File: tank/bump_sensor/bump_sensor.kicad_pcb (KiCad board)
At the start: 2 copper layers, 77.5 x 11.2 mm, 5 parts, among them J1 Conn_01x02_Male, SW1 SW_SPDT, SW2 SW_SPDT

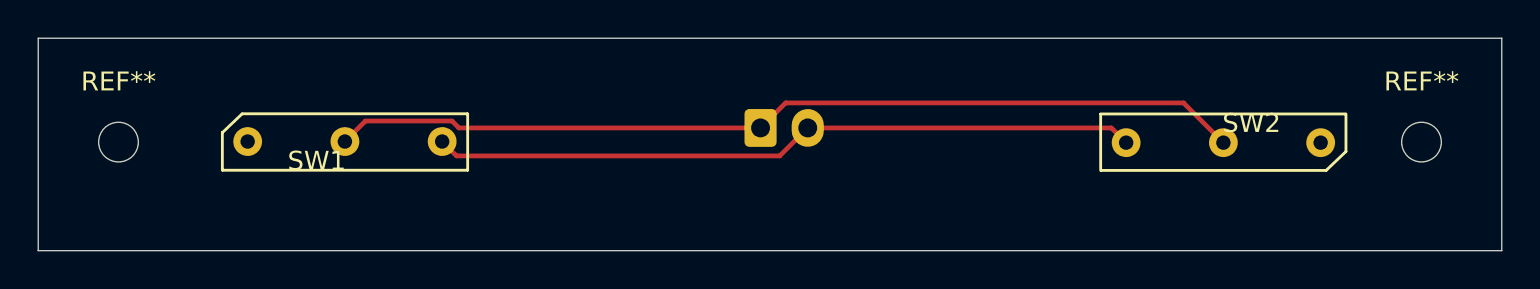
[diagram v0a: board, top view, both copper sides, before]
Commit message: Bump Sensor Version 0.2 - make contact switch thru-holes bigger
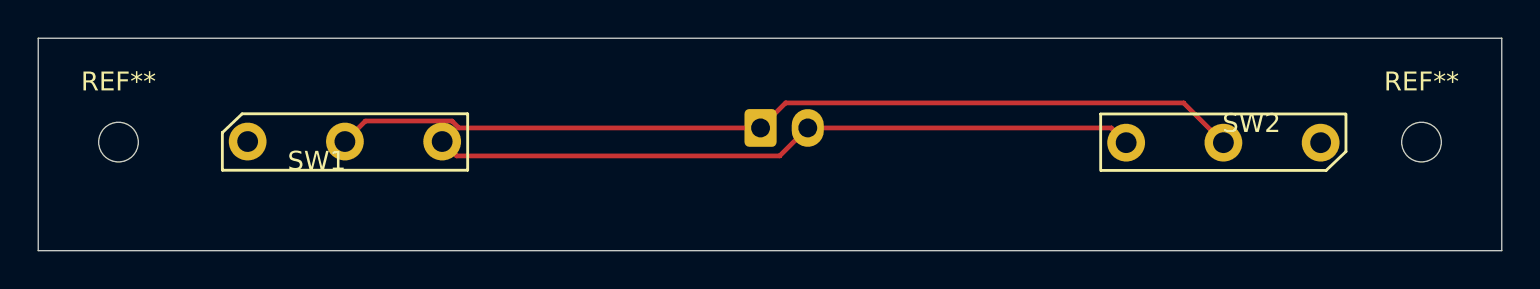
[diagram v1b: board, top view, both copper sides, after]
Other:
- board text added: "Laser Tag Robot Tank Bump Sensor 0.2 M.I.A.R. Labs nick.groesz@gmail.com"
- board text removed: "Laser Tag Robot Tank Bump Sensor 0.1 M.I.A.R. Labs nick.groesz@gmail.com"

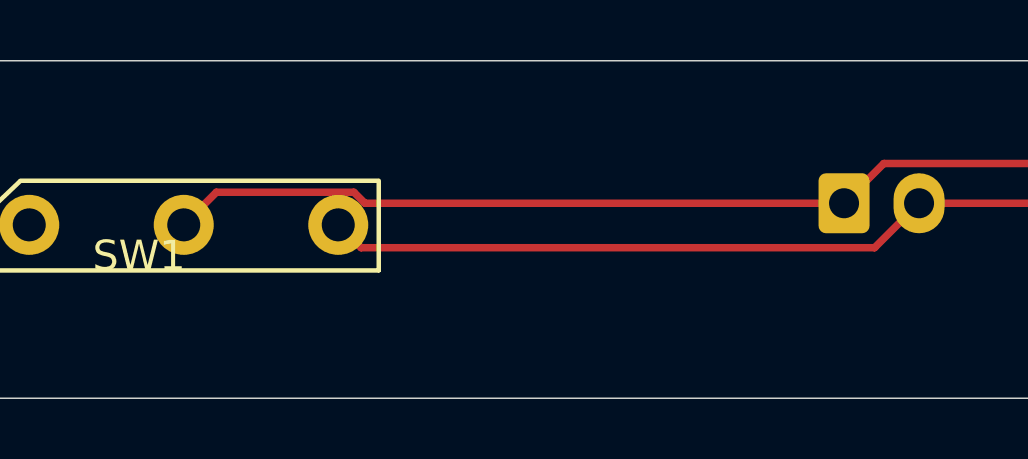
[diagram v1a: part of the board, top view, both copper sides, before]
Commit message: I cannot believe that I screwed-up the Bump Sensor in such a dumb way and failed to run the design rule checker
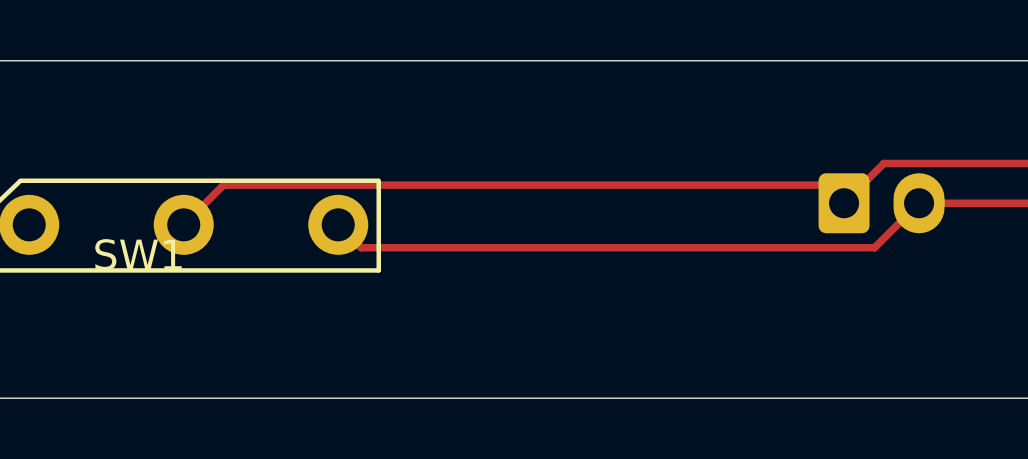
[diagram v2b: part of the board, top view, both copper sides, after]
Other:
- board text added: "Laser Tag Robot Tank Bump Sensor 0.3 M.I.A.R. Labs nick.groesz@gmail.com"
- board text removed: "Laser Tag Robot Tank Bump Sensor 0.2 M.I.A.R. Labs nick.groesz@gmail.com"
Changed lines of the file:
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@@
-(kicad_pcb (version 20171130) (host pcbnew 5.1.7-a382d34a8~88~ubuntu18.04.1)
+(kicad_pcb (version 20171130) (host pcbnew 5.1.12-84ad8e8a86~92~ubuntu20.04.1)
   (general
     (thickness 1.6)
     (drawings 5)
-    (tracks 12)
+    (tracks 11)
     (zones 0)
     (modules 5)
@@
       (effects (font (size 1 1) (thickness 0.15)))
     )
-    (fp_line (start -4.05 -2.1) (end -5.1 -1.08) (layer F.CrtYd) (width 0.05))
+    (fp_line (start -5.1 1.1) (end 8.1 1.1) (layer F.CrtYd) (width 0.05))
+    (fp_line (start 8.1 -2.1) (end 8.1 1.1) (layer F.CrtYd) (width 0.05))
+    (fp_line (start -4.02 -2.11) (end 8.1 -2.11) (layer F.CrtYd) (width 0.05))
+    (fp_line (start -5.1 -1.08) (end -5.1 1.1) (layer F.CrtYd) (width 0.05))
+    (fp_line (start -4.99 0.99) (end 7.99 0.99) (layer F.SilkS) (width 0.15))
+    (fp_line (start -5 0.98) (end -5 -1.01) (layer F.SilkS) (width 0.15))
+    (fp_line (start -3.95 -2) (end 7.95 -2) (layer F.SilkS) (width 0.15))
+    (fp_line (start 7.99 -2) (end 7.99 0.98) (layer F.SilkS) (width 0.15))
     (fp_line (start -5 -1) (end -3.96 -1.99) (layer F.SilkS) (width 0.15))
-    (fp_line (start 7.99 -2) (end 7.99 0.98) (layer F.SilkS) (width 0.15))
-    (fp_line (start -3.95 -2) (end 7.95 -2) (layer F.SilkS) (width 0.15))
-    (fp_line (start -5 0.98) (end -5 -1.01) (layer F.SilkS) (width 0.15))
-    (fp_line (start -4.99 0.99) (end 7.99 0.99) (layer F.SilkS) (width 0.15))
-    (fp_line (start -5.1 -1.08) (end -5.1 1.06) (layer F.CrtYd) (width 0.05))
-    (fp_line (start -4.04 -2.1) (end 8.11 -2.11) (layer F.CrtYd) (width 0.05))
-    (fp_line (start 8.1 -2.1) (end 8.1 1.11) (layer F.CrtYd) (width 0.05))
-    (fp_line (start -5.1 1.1) (end 8.11 1.1) (layer F.CrtYd) (width 0.05))
+    (fp_line (start -4.02 -2.11) (end -5.1 -1.08) (layer F.CrtYd) (width 0.05))
     (pad 1 thru_hole circle (at -3.66 -0.53) (size 2 2) (drill 1.1) (layers *.Cu *.Mask)
       (net 3 "Net-(SW1-Pad1)"))
@@
       (effects (font (size 1 1) (thickness 0.15)))
     )
+    (fp_circle (center 0 0) (end 2.35 0) (layer F.CrtYd) (width 0.05))
     (fp_circle (center 0 0) (end 2.1 0) (layer Cmts.User) (width 0.15))
-    (fp_circle (center 0 0) (end 2.35 0) (layer F.CrtYd) (width 0.05))
     (fp_text user %R (at 0.3 0) (layer F.Fab)
       (effects (font (size 1 1) (thickness 0.15)))
@@
       (effects (font (size 1 1) (thickness 0.15)))
     )
+    (fp_circle (center 0 0) (end 2.35 0) (layer F.CrtYd) (width 0.05))
     (fp_circle (center 0 0) (end 2.1 0) (layer Cmts.User) (width 0.15))
-    (fp_circle (center 0 0) (end 2.35 0) (layer F.CrtYd) (width 0.05))
     (fp_text user %R (at 0.3 0) (layer F.Fab)
       (effects (font (size 1 1) (thickness 0.15)))
@@
       (effects (font (size 1 1) (thickness 0.15)) (justify mirror))
     )
+    (fp_line (start -2.5 1.6) (end -2.5 -2.2) (layer B.Fab) (width 0.1))
+    (fp_line (start -2.5 -2.2) (end 5 -2.2) (layer B.Fab) (width 0.1))
+    (fp_line (start 5 -2.2) (end 5 1.6) (layer B.Fab) (width 0.1))
+    (fp_line (start 5 1.6) (end -2.5 1.6) (layer B.Fab) (width 0.1))
+    (fp_line (start -3 2.1) (end -3 -2.7) (layer B.CrtYd) (width 0.05))
+    (fp_line (start -3 -2.7) (end 5.5 -2.7) (layer B.CrtYd) (width 0.05))
+    (fp_line (start 5.5 -2.7) (end 5.5 2.1) (layer B.CrtYd) (width 0.05))
+    (fp_line (start 5.5 2.1) (end -3 2.1) (layer B.CrtYd) (width 0.05))
+    (fp_line (start -2.61 1.71) (end -2.61 -2.31) (layer B.SilkS) (width 0.12))
+    (fp_line (start -2.61 -2.31) (end 5.11 -2.31) (layer B.SilkS) (width 0.12))
+    (fp_line (start 5.11 -2.31) (end 5.11 1.71) (layer B.SilkS) (width 0.12))
+    (fp_line (start 5.11 1.71) (end -2.61 1.71) (layer B.SilkS) (width 0.12))
+    (fp_line (start -2.61 0) (end -2.11 0) (layer B.SilkS) (width 0.12))
+    (fp_line (start -2.11 0) (end -2.11 1.21) (layer B.SilkS) (width 0.12))
+    (fp_line (start -2.11 1.21) (end 4.61 1.21) (layer B.SilkS) (width 0.12))
+    (fp_line (start 4.61 1.21) (end 4.61 0) (layer B.SilkS) (width 0.12))
+    (fp_line (start 4.61 0) (end 5.11 0) (layer B.SilkS) (width 0.12))
+    (fp_line (start -2.61 -0.81) (end -1.61 -0.81) (layer B.SilkS) (width 0.12))
+    (fp_line (start -1.61 -0.81) (end -1.61 -2.31) (layer B.SilkS) (width 0.12))
+    (fp_line (start 5.11 -0.81) (end 4.11 -0.81) (layer B.SilkS) (width 0.12))
+    (fp_line (start 4.11 -0.81) (end 4.11 -2.31) (layer B.SilkS) (width 0.12))
+    (fp_line (start -2.91 -0.11) (end -2.91 -2.61) (layer B.SilkS) (width 0.12))
+    (fp_line (start -2.91 -2.61) (end -0.41 -2.61) (layer B.SilkS) (width 0.12))
+    (fp_line (start -2.91 -0.11) (end -2.91 -2.61) (layer B.Fab) (width 0.1))
     (fp_line (start -2.91 -2.61) (end -0.41 -2.61) (layer B.Fab) (width 0.1))
-    (fp_line (start -2.91 -0.11) (end -2.91 -2.61) (layer B.Fab) (width 0.1))
-    (fp_line (start -2.91 -2.61) (end -0.41 -2.61) (layer B.SilkS) (width 0.12))
-    (fp_line (start -2.91 -0.11) (end -2.91 -2.61) (layer B.SilkS) (width 0.12))
-    (fp_line (start 4.11 -0.81) (end 4.11 -2.31) (layer B.SilkS) (width 0.12))
-    (fp_line (start 5.11 -0.81) (end 4.11 -0.81) (layer B.SilkS) (width 0.12))
-    (fp_line (start -1.61 -0.81) (end -1.61 -2.31) (layer B.SilkS) (width 0.12))
-    (fp_line (start -2.61 -0.81) (end -1.61 -0.81) (layer B.SilkS) (width 0.12))
-    (fp_line (start 4.61 0) (end 5.11 0) (layer B.SilkS) (width 0.12))
-    (fp_line (start 4.61 1.21) (end 4.61 0) (layer B.SilkS) (width 0.12))
-    (fp_line (start -2.11 1.21) (end 4.61 1.21) (layer B.SilkS) (width 0.12))
-    (fp_line (start -2.11 0) (end -2.11 1.21) (layer B.SilkS) (width 0.12))
-    (fp_line (start -2.61 0) (end -2.11 0) (layer B.SilkS) (width 0.12))
-    (fp_line (start 5.11 1.71) (end -2.61 1.71) (layer B.SilkS) (width 0.12))
-    (fp_line (start 5.11 -2.31) (end 5.11 1.71) (layer B.SilkS) (width 0.12))
-    (fp_line (start -2.61 -2.31) (end 5.11 -2.31) (layer B.SilkS) (width 0.12))
-    (fp_line (start -2.61 1.71) (end -2.61 -2.31) (layer B.SilkS) (width 0.12))
-    (fp_line (start 5.5 2.1) (end -3 2.1) (layer B.CrtYd) (width 0.05))
-    (fp_line (start 5.5 -2.7) (end 5.5 2.1) (layer B.CrtYd) (width 0.05))
-    (fp_line (start -3 -2.7) (end 5.5 -2.7) (layer B.CrtYd) (width 0.05))
-    (fp_line (start -3 2.1) (end -3 -2.7) (layer B.CrtYd) (width 0.05))
-    (fp_line (start 5 1.6) (end -2.5 1.6) (layer B.Fab) (width 0.1))
-    (fp_line (start 5 -2.2) (end 5 1.6) (layer B.Fab) (width 0.1))
-    (fp_line (start -2.5 -2.2) (end 5 -2.2) (layer B.Fab) (width 0.1))
-    (fp_line (start -2.5 1.6) (end -2.5 -2.2) (layer B.Fab) (width 0.1))
     (fp_text user %R (at 1.25 -1.5) (layer B.Fab)
       (effects (font (size 1 1) (thickness 0.15)) (justify mirror))
@@
     )
   )
-  (gr_text "Laser Tag Robot Tank\nBump Sensor 0.2\nM.I.A.R. Labs\nnick.groesz@gmail.com" (at 71.25 106.75) (layer B.SilkS)
+  (gr_text "Laser Tag Robot Tank\nBump Sensor 0.3\nM.I.A.R. Labs\nnick.groesz@gmail.com" (at 71.25 106.75) (layer B.SilkS)
     (effects (font (size 1 1) (thickness 0.15)) (justify mirror))
   )
@@
   (gr_line (start 97.75 101.75) (end 97.75 113) (layer Edge.Cuts) (width 0.05))
   (gr_line (start 20.25 101.75) (end 97.75 101.75) (layer Edge.Cuts) (width 0.05))
-  (segment (start 37.577001 106.132999) (end 36.49 107.22) (width 0.25) (layer F.Cu) (net 1))
-  (segment (start 42.161761 106.132999) (end 37.577001 106.132999) (width 0.25) (layer F.Cu) (net 1))
-  (segment (start 42.528762 106.5) (end 42.161761 106.132999) (width 0.25) (layer F.Cu) (net 1))
-  (segment (start 58.5 106.5) (end 42.528762 106.5) (width 0.25) (layer F.Cu) (net 1))
   (segment (start 59.82501 105.17499) (end 58.5 106.5) (width 0.25) (layer F.Cu) (net 1))
   (segment (start 80.90499 105.17499) (end 59.82501 105.17499) (width 0.25) (layer F.Cu) (net 1))
   (segment (start 83.01 107.28) (end 80.90499 105.17499) (width 0.25) (layer F.Cu) (net 1))
+  (segment (start 37.815001 105.894999) (end 36.49 107.22) (width 0.25) (layer F.Cu) (net 1))
+  (segment (start 57.894999 105.894999) (end 37.815001 105.894999) (width 0.25) (layer F.Cu) (net 1))
+  (segment (start 58.5 106.5) (end 57.894999 105.894999) (width 0.25) (layer F.Cu) (net 1))
   (segment (start 59.518001 107.981999) (end 61 106.5) (width 0.25) (layer F.Cu) (net 2))
   (segment (start 42.401999 107.981999) (end 59.518001 107.981999) (width 0.25) (layer F.Cu) (net 2))

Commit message: Major cleanup. I localized all the footprint and symbol libraries.
I deleted most of the rescue stuff.

I still need to finish-up changes to the turret board.

Now this checkout should work "out of the box".
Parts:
- J1: footprint Connector_JST:JST_EH_B2B-EH-A_1x02_P2.50mm_Vertical -> custom:JST_EH_B2B-EH-A_1x02_P2.50mm_Vertical
- SW1, SW2: footprint Custom:micro_switch -> custom:micro_switch
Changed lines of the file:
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@@
     (add_net "Net-(SW2-Pad1)")
-  )
-  (module Custom:micro_switch (layer F.Cu)
-    (at 84.5 106.75 180)
-    (fp_text reference SW2 (at 0 0.5) (layer F.SilkS)
-      (effects (font (size 1 1) (thickness 0.15)))
-    )
-    (fp_text value SW_SPDT (at 0 -0.5) (layer F.Fab)
-      (effects (font (size 1 1) (thickness 0.15)))
-    )
-    (fp_line (start -4.05 -2.1) (end -5.1 -1.08) (layer F.CrtYd) (width 0.05))
-    (fp_line (start -5 -1) (end -3.96 -1.99) (layer F.SilkS) (width 0.15))
-    (fp_line (start 7.99 -2) (end 7.99 0.98) (layer F.SilkS) (width 0.15))
-    (fp_line (start -3.95 -2) (end 7.95 -2) (layer F.SilkS) (width 0.15))
-    (fp_line (start -5 0.98) (end -5 -1.01) (layer F.SilkS) (width 0.15))
-    (fp_line (start -4.99 0.99) (end 7.99 0.99) (layer F.SilkS) (width 0.15))
-    (fp_line (start -5.1 -1.08) (end -5.1 1.06) (layer F.CrtYd) (width 0.05))
-    (fp_line (start -4.04 -2.1) (end 8.11 -2.11) (layer F.CrtYd) (width 0.05))
-    (fp_line (start 8.1 -2.1) (end 8.1 1.11) (layer F.CrtYd) (width 0.05))
-    (fp_line (start -5.1 1.1) (end 8.11 1.1) (layer F.CrtYd) (width 0.05))
-    (pad 3 thru_hole circle (at 6.64 -0.53 180) (size 2 2) (drill 1.1) (layers *.Cu *.Mask)
-      (net 2 "Net-(J1-Pad2)"))
-    (pad 2 thru_hole circle (at 1.49 -0.53 180) (size 2 2) (drill 1.1) (layers *.Cu *.Mask)
-      (net 1 "Net-(J1-Pad1)"))
-    (pad 1 thru_hole circle (at -3.66 -0.53 180) (size 2 2) (drill 1.1) (layers *.Cu *.Mask)
-      (net 4 "Net-(SW2-Pad1)"))
-  )
-  (module Custom:micro_switch (layer F.Cu)
-    (at 35 107.75)
-    (fp_text reference SW1 (at 0 0.5) (layer F.SilkS)
-      (effects (font (size 1 1) (thickness 0.15)))
-    )
-    (fp_text value SW_SPDT (at 0 -0.5) (layer F.Fab)
-      (effects (font (size 1 1) (thickness 0.15)))
-    )
-    (fp_line (start -5.1 1.1) (end 8.1 1.1) (layer F.CrtYd) (width 0.05))
-    (fp_line (start 8.1 -2.1) (end 8.1 1.1) (layer F.CrtYd) (width 0.05))
-    (fp_line (start -4.02 -2.11) (end 8.1 -2.11) (layer F.CrtYd) (width 0.05))
-    (fp_line (start -5.1 -1.08) (end -5.1 1.1) (layer F.CrtYd) (width 0.05))
-    (fp_line (start -4.99 0.99) (end 7.99 0.99) (layer F.SilkS) (width 0.15))
-    (fp_line (start -5 0.98) (end -5 -1.01) (layer F.SilkS) (width 0.15))
-    (fp_line (start -3.95 -2) (end 7.95 -2) (layer F.SilkS) (width 0.15))
-    (fp_line (start 7.99 -2) (end 7.99 0.98) (layer F.SilkS) (width 0.15))
-    (fp_line (start -5 -1) (end -3.96 -1.99) (layer F.SilkS) (width 0.15))
-    (fp_line (start -4.02 -2.11) (end -5.1 -1.08) (layer F.CrtYd) (width 0.05))
-    (pad 1 thru_hole circle (at -3.66 -0.53) (size 2 2) (drill 1.1) (layers *.Cu *.Mask)
-      (net 3 "Net-(SW1-Pad1)"))
-    (pad 2 thru_hole circle (at 1.49 -0.53) (size 2 2) (drill 1.1) (layers *.Cu *.Mask)
-      (net 1 "Net-(J1-Pad1)"))
-    (pad 3 thru_hole circle (at 6.64 -0.53) (size 2 2) (drill 1.1) (layers *.Cu *.Mask)
-      (net 2 "Net-(J1-Pad2)"))
   )
   (module MountingHole:MountingHole_2.1mm (layer F.Cu)
@@
     (tags "mounting hole 2.1mm no annular")
     (attr virtual)
-    (fp_text reference REF** (at 0 -3.2) (layer F.SilkS)
+    (fp_text reference REF** (at 0 -3.2) (layer F.SilkS) hide
       (effects (font (size 1 1) (thickness 0.15)))
     )
@@
       (effects (font (size 1 1) (thickness 0.15)))
     )
+    (fp_circle (center 0 0) (end 2.1 0) (layer Cmts.User) (width 0.15))
     (fp_circle (center 0 0) (end 2.35 0) (layer F.CrtYd) (width 0.05))
-    (fp_circle (center 0 0) (end 2.1 0) (layer Cmts.User) (width 0.15))
     (fp_text user %R (at 0.3 0) (layer F.Fab)
       (effects (font (size 1 1) (thickness 0.15)))
@@
     (tags "mounting hole 2.1mm no annular")
     (attr virtual)
-    (fp_text reference REF** (at 0 -3.2) (layer F.SilkS)
+    (fp_text reference REF** (at 0 -3.2) (layer F.SilkS) hide
       (effects (font (size 1 1) (thickness 0.15)))
     )
@@
       (effects (font (size 1 1) (thickness 0.15)))
     )
+    (fp_circle (center 0 0) (end 2.1 0) (layer Cmts.User) (width 0.15))
     (fp_circle (center 0 0) (end 2.35 0) (layer F.CrtYd) (width 0.05))
-    (fp_circle (center 0 0) (end 2.1 0) (layer Cmts.User) (width 0.15))
     (fp_text user %R (at 0.3 0) (layer F.Fab)
       (effects (font (size 1 1) (thickness 0.15)))
@@
     (pad "" np_thru_hole circle (at 0 0) (size 2.1 2.1) (drill 2.1) (layers *.Cu *.Mask))
   )
-  (module Connector_JST:JST_EH_B2B-EH-A_1x02_P2.50mm_Vertical (layer B.Cu)
+  (module custom:JST_EH_B2B-EH-A_1x02_P2.50mm_Vertical (layer B.Cu)
     (at 58.5 106.5)
     (descr "JST EH series connector, B2B-EH-A (http://www.jst-mfg.com/product/pdf/eng/eEH.pdf), generated with kicad-footprint-generator")
@@
       (effects (font (size 1 1) (thickness 0.15)) (justify mirror))
     )
-    (fp_text value Conn_01x02_Male (at 1.25 -3.4) (layer B.Fab)
+    (fp_text value Conn_01x02_Male (at 1.25 -3.4) (layer B.SilkS)
       (effects (font (size 1 1) (thickness 0.15)) (justify mirror))
     )
@@
     (pad 2 thru_hole oval (at 2.5 0) (size 1.7 2) (drill 1) (layers *.Cu *.Mask)
       (net 2 "Net-(J1-Pad2)"))
-    (model ${KISYS3DMOD}/Connector_JST.3dshapes/JST_EH_B2B-EH-A_1x02_P2.50mm_Vertical.wrl
+    (model ${KICAD6_3DMODEL_DIR}/Connector_JST.3dshapes/JST_EH_B2B-EH-A_1x02_P2.50mm_Vertical.wrl
       (at (xyz 0 0 0))
       (scale (xyz 1 1 1))
@@
     )
   )
+  (module custom:micro_switch (layer F.Cu)
+    (at 35 107.75)
+    (fp_text reference SW1 (at 0 0.5) (layer F.SilkS)
+      (effects (font (size 1 1) (thickness 0.15)))
+    )
+    (fp_text value SW_SPDT (at 0 -0.5) (layer F.Fab)
+      (effects (font (size 1 1) (thickness 0.15)))
+    )
+    (fp_line (start -5.1 1.1) (end 8.1 1.1) (layer F.CrtYd) (width 0.05))
+    (fp_line (start 8.1 -2.1) (end 8.1 1.1) (layer F.CrtYd) (width 0.05))
+    (fp_line (start -4.02 -2.11) (end 8.1 -2.11) (layer F.CrtYd) (width 0.05))
+    (fp_line (start -5.1 -1.08) (end -5.1 1.1) (layer F.CrtYd) (width 0.05))
+    (fp_line (start -4.99 0.99) (end 7.99 0.99) (layer F.SilkS) (width 0.15))
+    (fp_line (start -5 0.98) (end -5 -1.01) (layer F.SilkS) (width 0.15))
+    (fp_line (start -3.95 -2) (end 7.95 -2) (layer F.SilkS) (width 0.15))
+    (fp_line (start 7.99 -2) (end 7.99 0.98) (layer F.SilkS) (width 0.15))
+    (fp_line (start -5 -1) (end -3.96 -1.99) (layer F.SilkS) (width 0.15))
+    (fp_line (start -4.02 -2.11) (end -5.1 -1.08) (layer F.CrtYd) (width 0.05))
+    (pad 1 thru_hole circle (at -3.66 -0.53) (size 2 2) (drill 1.1) (layers *.Cu *.Mask)
+      (net 3 "Net-(SW1-Pad1)"))
+    (pad 2 thru_hole circle (at 1.49 -0.53) (size 2 2) (drill 1.1) (layers *.Cu *.Mask)
+      (net 1 "Net-(J1-Pad1)"))
+    (pad 3 thru_hole circle (at 6.64 -0.53) (size 2 2) (drill 1.1) (layers *.Cu *.Mask)
+      (net 2 "Net-(J1-Pad2)"))
+  )
+  (module custom:micro_switch (layer F.Cu)
+    (at 84.5 106.75 180)
+    (fp_text reference SW2 (at 0 0.5) (layer F.SilkS)
+      (effects (font (size 1 1) (thickness 0.15)))
+    )
+    (fp_text value SW_SPDT (at 0 -0.5) (layer F.Fab)
+      (effects (font (size 1 1) (thickness 0.15)))
+    )
+    (fp_line (start -4.02 -2.11) (end -5.1 -1.08) (layer F.CrtYd) (width 0.05))
+    (fp_line (start -5 -1) (end -3.96 -1.99) (layer F.SilkS) (width 0.15))
+    (fp_line (start 7.99 -2) (end 7.99 0.98) (layer F.SilkS) (width 0.15))
+    (fp_line (start -3.95 -2) (end 7.95 -2) (layer F.SilkS) (width 0.15))
+    (fp_line (start -5 0.98) (end -5 -1.01) (layer F.SilkS) (width 0.15))
+    (fp_line (start -4.99 0.99) (end 7.99 0.99) (layer F.SilkS) (width 0.15))
+    (fp_line (start -5.1 -1.08) (end -5.1 1.1) (layer F.CrtYd) (width 0.05))
+    (fp_line (start -4.02 -2.11) (end 8.1 -2.11) (layer F.CrtYd) (width 0.05))
+    (fp_line (start 8.1 -2.1) (end 8.1 1.1) (layer F.CrtYd) (width 0.05))
+    (fp_line (start -5.1 1.1) (end 8.1 1.1) (layer F.CrtYd) (width 0.05))
+    (pad 3 thru_hole circle (at 6.64 -0.53 180) (size 2 2) (drill 1.1) (layers *.Cu *.Mask)
+      (net 2 "Net-(J1-Pad2)"))
+    (pad 2 thru_hole circle (at 1.49 -0.53 180) (size 2 2) (drill 1.1) (layers *.Cu *.Mask)
+      (net 1 "Net-(J1-Pad1)"))
+    (pad 1 thru_hole circle (at -3.66 -0.53 180) (size 2 2) (drill 1.1) (layers *.Cu *.Mask)
+      (net 4 "Net-(SW2-Pad1)"))
+  )
   (gr_text "Laser Tag Robot Tank\nBump Sensor 0.3\nM.I.A.R. Labs\nnick.groesz@gmail.com" (at 71.25 106.75) (layer B.SilkS)
